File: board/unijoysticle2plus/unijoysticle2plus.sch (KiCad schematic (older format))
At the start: 39 parts, among them J1 DB9_Female, J2 DB9_Female, J3 USB_B_Micro, Q1 MUN5211DW1, SW1 RESET, SW2 JOY SWAP, SW3 BOOT, U1 74HC05, U2 74HC05, U3 74HC05, U4 ESP32-WROOM-32D, U5 AMS1117-3.3, U6 CH340C

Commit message: unijoysticle2plus: rev C
Rev C submitted to JLCPCB.
Added missing JLCPCB parts
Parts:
- C10: LCSC (none) -> C28323
- Q1: LCSC (none) -> C152507
- R5, R6: value 1K -> 1k
- U4: value ESP32-WROOM-32D -> ESP32-WROOM-32E; LCSC C473012 -> C701342
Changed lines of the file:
@@
 P 5250 2750
 F 0 "U4" H 5800 1350 50  0000 C CNN
-F 1 "ESP32-WROOM-32D" H 5850 1250 50  0000 C CNN
+F 1 "ESP32-WROOM-32E" H 5850 1250 50  0000 C CNN
 F 2 "RF_Module:ESP32-WROOM-32" H 5250 1250 50  0001 C CNN
 F 3 "https://www.espressif.com/sites/default/files/documentation/esp32-wroom-32d_esp32-wroom-32u_datasheet_en.pdf" H 4950 2800 50  0001 C CNN
-F 4 "C473012" H 5250 2750 50  0001 C CNN "LCSC"
+F 4 "C701342" H 5250 2750 50  0001 C CNN "LCSC"
 	1    5250 2750
 	1    0    0    -1
@@
 P 10180 2340
 F 0 "R5" V 10040 2340 50  0000 C CNN
-F 1 "1K" V 10110 2340 50  0000 C CNN
+F 1 "1k" V 10110 2340 50  0000 C CNN
 F 2 "Resistor_SMD:R_0805_2012Metric_Pad1.20x1.40mm_HandSolder" H 10180 2340 50  0001 C CNN
 F 3 "~" H 10180 2340 50  0001 C CNN
@@
 P 10180 2440
 F 0 "R6" V 10250 2440 50  0000 C CNN
-F 1 "1K" V 10310 2440 50  0000 C CNN
+F 1 "1k" V 10310 2440 50  0000 C CNN
 F 2 "Resistor_SMD:R_0805_2012Metric_Pad1.20x1.40mm_HandSolder" H 10180 2440 50  0001 C CNN
 F 3 "~" H 10180 2440 50  0001 C CNN
@@
 F 2 "Package_TO_SOT_SMD:SOT-363_SC-70-6" H 7825 4390 50  0001 C CNN
 F 3 "http://www.onsemi.com/pub/Collateral/DTC114ED-D.PDF" H 7820 4830 50  0001 C CNN
+F 4 "C152507" H 7820 4830 50  0001 C CNN "LCSC"
 	1    7820 4830
 	1    0    0    1
@@
 Wire Wire Line
 	8800 1950 8800 1980
-$Comp
-L Device:C_Small C10
-U 1 1 61070B93
-P 8990 2080
-F 0 "C10" H 9082 2126 50  0000 L CNN
-F 1 "1uF" H 9082 2035 50  0000 L CNN
-F 2 "Capacitor_SMD:C_0805_2012Metric_Pad1.18x1.45mm_HandSolder" H 8990 2080 50  0001 C CNN
-F 3 "~" H 8990 2080 50  0001 C CNN
-	1    8990 2080
-	1    0    0    -1
-$EndComp
 Wire Wire Line
 	8990 2180 8990 2210
@@
 	1    0    0    -1
 $EndComp
+$Comp
+L Device:C_Small C10
+U 1 1 61070B93
+P 8990 2080
+F 0 "C10" H 9082 2126 50  0000 L CNN
+F 1 "1uF" H 9082 2035 50  0000 L CNN
+F 2 "Capacitor_SMD:C_0805_2012Metric_Pad1.18x1.45mm_HandSolder" H 8990 2080 50  0001 C CNN
+F 3 "~" H 8990 2080 50  0001 C CNN
+F 4 "C28323" H 8990 2080 50  0001 C CNN "LCSC"
+	1    8990 2080
+	1    0    0    -1
+$EndComp

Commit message: Unijoysticle2+: Rev D
- Swap GPIO 12 & 13: issue #19
- Ground GPIO 4. This is to detect Uni2+
- Back to USB Micro B connector used in Rev. B
  - This is to avoid hand-soldering it.
  - Re-added the "hole" in PCB so that it can be placed using P&P
    machine.
- Reduced Green LED resistor from 1k to 330, this is to make it
  brighter.
- Auto reset circuit wasn't working on Rev C.
  Replaced it with original design, using S8050s.
  Fixed the pins, was broken in Rev A and Rev B.
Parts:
- removed Q1: MUN5211DW1, Package_TO_SOT_SMD:SOT-363_SC-70-6, symbol Transistor_BJT:MUN5211DW1
- added Q1, Q2: S8050, Package_TO_SOT_SMD:SOT-23, symbol Device:Q_NPN_BEC
- added R7, R8: 10k, Resistor_SMD:R_0805_2012Metric_Pad1.20x1.40mm_HandSolder, symbol Device:R_Small
- J3: footprint Unijoysticle:MicroXNJ -> Connector_USB:USB_Micro-B_Molex_47346-0001; LCSC C404969 -> C132560
- R3: value 1k -> 330; LCSC C17513 -> C17630
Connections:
- wire segments 193 -> 198
- no-connect marks 19 -> 18
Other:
- note added: "Differenciates between\nUnijoysticle2 and Unijoysticle2+.\nTo only have one firmware"
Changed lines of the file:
@@
 Sheet 1 1
 Title "Unijoysticle 2+"
-Date "2021-06-25"
-Rev "C"
+Date "2021-07-24"
+Rev "D"
 Comp "Retro Moe"
 Comment1 ""
@@
 Text Label 6650 2050 2    50   ~ 0
 GPIO_J1_LED
-Text Label 6650 2250 2    50   ~ 0
+Text Label 6650 2150 2    50   ~ 0
 GPIO_J2_LED
 Text Label 6650 2450 2    50   ~ 0
@@
 Text Label 6650 3350 2    50   ~ 0
 GPIO_J1_UP
-Text Label 6650 2150 2    50   ~ 0
+Text Label 6650 2250 2    50   ~ 0
 GPIO_J2_FIRE
 Text Label 6650 2350 2    50   ~ 0
@@
 Text Label 6650 1950 2    50   ~ 0
 GPIO04
-Wire Wire Line
-	7130 2850 7130 2750
 Text Label 7860 2350 2    50   ~ 0
 USBD+
@@
 	1    0    0    -1
 $EndComp
-Wire Wire Line
-	7920 4480 7380 4480
-Wire Wire Line
-	7380 4480 7380 4830
-Connection ~ 7380 4830
-Wire Wire Line
-	7280 4280 7280 4630
-Wire Wire Line
-	7280 4280 6980 4280
-Connection ~ 7280 4280
-Wire Wire Line
-	6980 4830 7380 4830
-$Comp
-L Connector:USB_B_Micro J3
-U 1 1 5F99FD12
-P 7130 2350
-F 0 "J3" H 7187 2817 50  0000 C CNN
-F 1 "USB_B_Micro" H 7187 2726 50  0000 C CNN
-F 2 "Unijoysticle:MicroXNJ" H 7280 2300 50  0001 C CNN
-F 3 "~" H 7280 2300 50  0001 C CNN
-F 4 "C404969" H 7130 2350 50  0001 C CNN "LCSC"
-	1    7130 2350
-	1    0    0    -1
-$EndComp
 Text Label 6980 4280 0    50   ~ 0
 DTR_PROG
 Text Label 6980 4830 0    50   ~ 0
 RTS_PROG
-Text Label 8080 5030 0    50   ~ 0
+Text Label 8640 5270 0    50   ~ 0
 ESP_BOOT
-Text Label 8160 4080 0    50   ~ 0
+Text Label 8830 3840 0    50   ~ 0
 ESP_EN
 Wire Wire Line
@@
 GPIO39
 Wire Wire Line
-	9460 5710 9860 5710
-Wire Wire Line
-	9460 5810 9860 5810
-Wire Wire Line
-	9460 5910 9860 5910
-Wire Wire Line
-	9460 6010 9860 6010
-Wire Wire Line
-	9460 6110 9860 6110
-Text Label 9610 6010 0    50   ~ 0
+	10260 5880 10660 5880
+Wire Wire Line
+	10260 5980 10660 5980
+Wire Wire Line
+	10260 6080 10660 6080
+Wire Wire Line
+	10260 6180 10660 6180
+Text Label 10410 6080 0    50   ~ 0
 GPIO36
-Text Label 9610 6110 0    50   ~ 0
+Text Label 10410 6180 0    50   ~ 0
 GPIO39
-Text Label 9610 5710 0    50   ~ 0
+Text Label 8790 5880 0    50   ~ 0
 GPIO04
-Text Label 9610 5810 0    50   ~ 0
+Text Label 10410 5880 0    50   ~ 0
 GPIO34
-Text Label 9610 5910 0    50   ~ 0
+Text Label 10410 5980 0    50   ~ 0
 GPIO35
 Wire Wire Line
@@
 Wire Notes Line
 	6700 550  6700 5500
-Wire Wire Line
-	7280 4630 7870 4630
 $Comp
 L power:+3V3 #PWR013
@@
 Text Notes 550  3650 0    98   ~ 20
 C64 PORTS
-Text Notes 10640 5750 0    98   ~ 20
+Text Notes 10810 5640 0    98   ~ 20
 MISC
 Text Notes 500  4100 0    98   ~ 20
@@
 NoConn ~ 4650 3150
 NoConn ~ 4650 3250
-NoConn ~ 9460 5710
-NoConn ~ 9460 5810
-NoConn ~ 9460 5910
-NoConn ~ 9460 6010
-NoConn ~ 9460 6110
+NoConn ~ 10260 5880
+NoConn ~ 10260 5980
+NoConn ~ 10260 6080
+NoConn ~ 10260 6180
 $Comp
 L Graphic:Logo_Open_Hardware_Small #LOGO1
@@
 P 6550 6000
 F 0 "R3" V 6620 6000 50  0000 C CNN
-F 1 "1k" V 6460 6000 50  0000 C CNN
+F 1 "330" V 6460 6000 50  0000 C CNN
 F 2 "Resistor_SMD:R_0805_2012Metric_Pad1.20x1.40mm_HandSolder" V 6480 6000 50  0001 C CNN
 F 3 "~" H 6550 6000 50  0001 C CNN
-F 4 "C17513" V 6550 6000 50  0001 C CNN "LCSC"
+F 4 "C17630" V 6550 6000 50  0001 C CNN "LCSC"
 	1    6550 6000
 	0    -1   -1   0
@@
 	4100 1800 4100 1840
 Connection ~ 4100 1550
-Text Notes 9120 6310 0    50   ~ 0
+Text Notes 9920 6380 0    50   ~ 0
 Available GPIOs for future use.\nGPIOs 34-39 are Input only
 Wire Wire Line
@@
 	0    -1   -1   0
 $EndComp
-$Comp
-L Transistor_BJT:MUN5211DW1 Q1
-U 2 1 60E74B41
-P 7870 4280
-F 0 "Q1" H 8011 4326 50  0000 L CNN
-F 1 "MUN5211DW1" H 8011 4235 50  0000 L CNN
-F 2 "Package_TO_SOT_SMD:SOT-363_SC-70-6" H 7875 3840 50  0001 C CNN
-F 3 "http://www.onsemi.com/pub/Collateral/DTC114ED-D.PDF" H 7870 4280 50  0001 C CNN
-	2    7870 4280
-	1    0    0    -1
-$EndComp
-$Comp
-L Transistor_BJT:MUN5211DW1 Q1
-U 1 1 60E75D85
-P 7820 4830
-F 0 "Q1" H 7961 4784 50  0000 L CNN
-F 1 "MUN5211DW1" H 7961 4875 50  0000 L CNN
-F 2 "Package_TO_SOT_SMD:SOT-363_SC-70-6" H 7825 4390 50  0001 C CNN
-F 3 "http://www.onsemi.com/pub/Collateral/DTC114ED-D.PDF" H 7820 4830 50  0001 C CNN
-F 4 "C152507" H 7820 4830 50  0001 C CNN "LCSC"
-	1    7820 4830
-	1    0    0    1
-$EndComp
-Wire Wire Line
-	7870 5030 8450 5030
-Wire Wire Line
-	7380 4830 7470 4830
-Wire Wire Line
-	7280 4280 7520 4280
 Wire Wire Line
 	9610 2010 9610 2140
@@
 	1    0    0    -1
 $EndComp
-Wire Wire Line
-	7920 4080 8430 4080
 NoConn ~ 7030 2750
 $Comp
@@
 	1    0    0    -1
 $EndComp
+Wire Wire Line
+	6980 4830 7450 4830
+Wire Wire Line
+	6980 4280 7420 4280
+$Comp
+L Device:R_Small R7
+U 1 1 6103A444
+P 7640 4280
+F 0 "R7" V 7580 4280 50  0000 C CNN
+F 1 "10k" V 7710 4280 50  0000 C CNN
+F 2 "Resistor_SMD:R_0805_2012Metric_Pad1.20x1.40mm_HandSolder" H 7640 4280 50  0001 C CNN
+F 3 "~" H 7640 4280 50  0001 C CNN
+F 4 "C17414" V 7640 4280 50  0001 C CNN "LCSC"
+	1    7640 4280
+	0    1    1    0
+$EndComp
+$Comp
+L Device:R_Small R8
+U 1 1 6103B159
+P 7640 4830
+F 0 "R8" V 7570 4830 50  0000 C CNN
+F 1 "10k" V 7720 4830 50  0000 C CNN
+F 2 "Resistor_SMD:R_0805_2012Metric_Pad1.20x1.40mm_HandSolder" H 7640 4830 50  0001 C CNN
+F 3 "~" H 7640 4830 50  0001 C CNN
+F 4 "C17414" V 7640 4830 50  0001 C CNN "LCSC"
+	1    7640 4830
+	0    1    1    0
+$EndComp
+Wire Wire Line
+	7740 4280 8040 4280
+Wire Wire Line
+	7740 4830 8040 4830
+Wire Wire Line
+	8340 5030 8340 5270
+Wire Wire Line
+	8340 5270 9000 5270
+Wire Wire Line
+	8340 4080 8340 3840
+Wire Wire Line
+	8340 3840 9100 3840
+Connection ~ 7420 4280
+Wire Wire Line
+	7420 4280 7540 4280
+Wire Wire Line
+	7450 4830 7450 4480
+Wire Wire Line
+	7450 4480 8340 4480
+Connection ~ 7450 4830
+Wire Wire Line
+	7450 4830 7540 4830
+Wire Wire Line
+	8340 4630 7420 4630
+Wire Wire Line
+	7420 4280 7420 4630
+$Comp
+L Device:Q_NPN_BEC Q1
+U 1 1 6114C279
+P 8240 4280
+F 0 "Q1" H 8430 4326 50  0000 L CNN
+F 1 "S8050" H 8430 4235 50  0000 L CNN
+F 2 "Package_TO_SOT_SMD:SOT-23" H 8440 4380 50  0001 C CNN
+F 3 "~" H 8240 4280 50  0001 C CNN
+F 4 "C2146" H 8240 4280 50  0001 C CNN "LCSC"
+	1    8240 4280
+	1    0    0    -1
+$EndComp
+$Comp
+L Device:Q_NPN_BEC Q2
+U 1 1 6114CB1B
+P 8240 4830
+F 0 "Q2" H 8430 4876 50  0000 L CNN
+F 1 "S8050" H 8430 4785 50  0000 L CNN
+F 2 "Package_TO_SOT_SMD:SOT-23" H 8440 4930 50  0001 C CNN
+F 3 "~" H 8240 4830 50  0001 C CNN
+F 4 "C2146" H 8240 4830 50  0001 C CNN "LCSC"
+	1    8240 4830
+	1    0    0    -1
+$EndComp
+Wire Wire Line
+	8780 5880 8780 5980
+$Comp
+L power:GND #PWR0113
+U 1 1 61222325
+P 8780 5980
+F 0 "#PWR0113" H 8780 5730 50  0001 C CNN
+F 1 "GND" H 8785 5807 50  0000 C CNN
+F 2 "" H 8780 5980 50  0001 C CNN
+F 3 "" H 8780 5980 50  0001 C CNN
+	1    8780 5980
+	1    0    0    -1
+$EndComp
+Wire Wire Line
+	8780 5880 9060 5880
+Text Notes 8420 5780 0    50   ~ 0
+Differenciates between\nUnijoysticle2 and Unijoysticle2+.\nTo only have one firmware
+Wire Wire Line
+	7130 2750 7130 2850
+$Comp
+L Connector:USB_B_Micro J3
+U 1 1 6137E281
+P 7130 2350
+F 0 "J3" H 7187 2817 50  0000 C CNN
+F 1 "USB_B_Micro" H 7187 2726 50  0000 C CNN
+F 2 "Connector_USB:USB_Micro-B_Molex_47346-0001" H 7280 2300 50  0001 C CNN
+F 3 "~" H 7280 2300 50  0001 C CNN
+F 4 "C132560" H 7130 2350 50  0001 C CNN "LCSC"
+	1    7130 2350
+	1    0    0    -1
+$EndComp

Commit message: unijoysticle2+: place 1000uF cap differently
- Change footprint of 1000uF: bigger
- Place it slightly differently
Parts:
- C7: footprint Capacitor_SMD:CP_Elec_8x10 -> Capacitor_SMD:CP_Elec_10x10; LCSC C134755 -> C249594
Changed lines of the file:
@@
 F 0 "C7" H 6200 1100 50  0000 L CNN
 F 1 "1000uF" H 6150 1000 50  0000 L CNN
-F 2 "Capacitor_SMD:CP_Elec_8x10" H 6400 1050 50  0001 C CNN
+F 2 "Capacitor_SMD:CP_Elec_10x10" H 6400 1050 50  0001 C CNN
 F 3 "~" H 6400 1050 50  0001 C CNN
-F 4 "C134755" H 6400 1050 50  0001 C CNN "LCSC"
+F 4 "C249594" H 6400 1050 50  0001 C CNN "LCSC"
 	1    6400 1050
 	1    0    0    -1

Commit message: Unijosyticle2+: ESP32-WROOM-32E Out-of-Stock, using D
JLCPCB doesn't have WROOM-32E in stock.
Switching back to 32D
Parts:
- U4: LCSC C701342 -> C473012
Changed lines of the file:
@@
 F 2 "RF_Module:ESP32-WROOM-32" H 5250 1250 50  0001 C CNN
 F 3 "https://www.espressif.com/sites/default/files/documentation/esp32-wroom-32d_esp32-wroom-32u_datasheet_en.pdf" H 4950 2800 50  0001 C CNN
-F 4 "C701342" H 5250 2750 50  0001 C CNN "LCSC"
+F 4 "C473012" H 5250 2750 50  0001 C CNN "LCSC"
 	1    5250 2750
 	1    0    0    -1

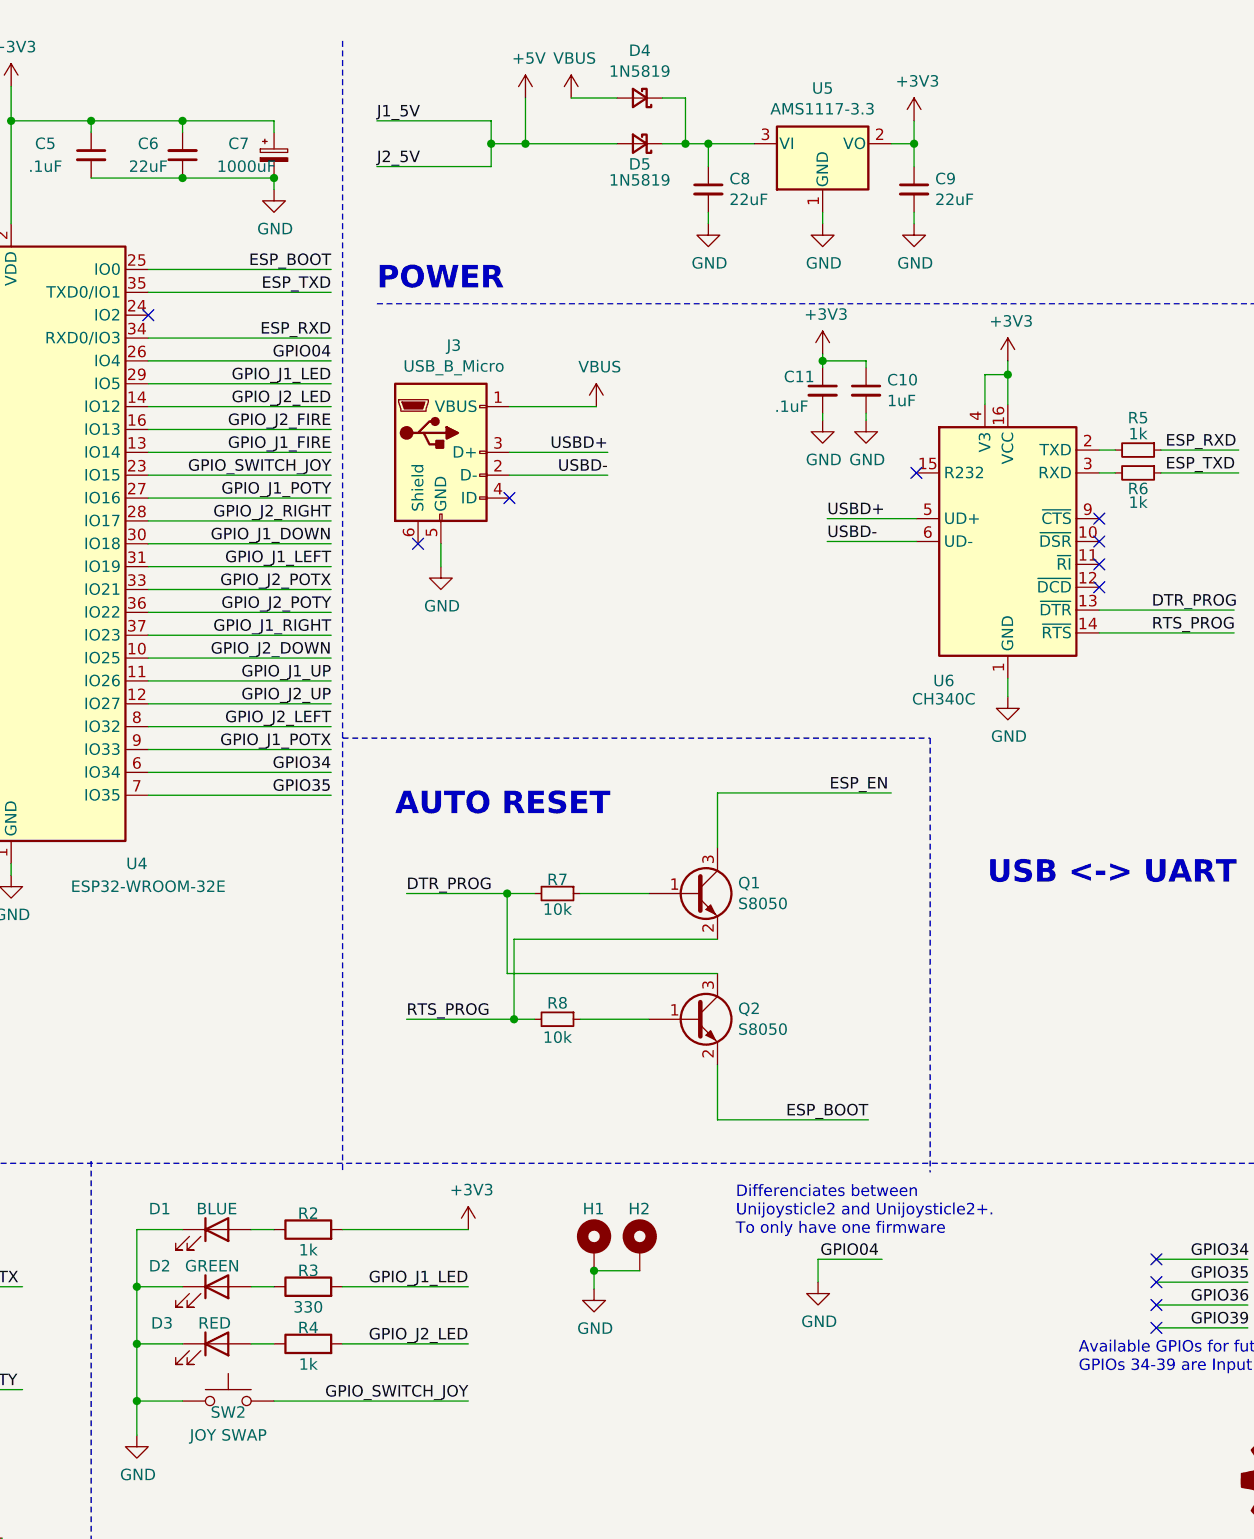
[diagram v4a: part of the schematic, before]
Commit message: Unijoysticle2+: Rev E
- Auto-reset circuit fixed: Transitor lines connected correctly
- Filter cap is between 5v and GND (and not +3.v3 and GND)
- Using 1.5K Ohm resistors for blue and red LEDs instead of 1K
- USB connector is just a tiny bit moved inwards
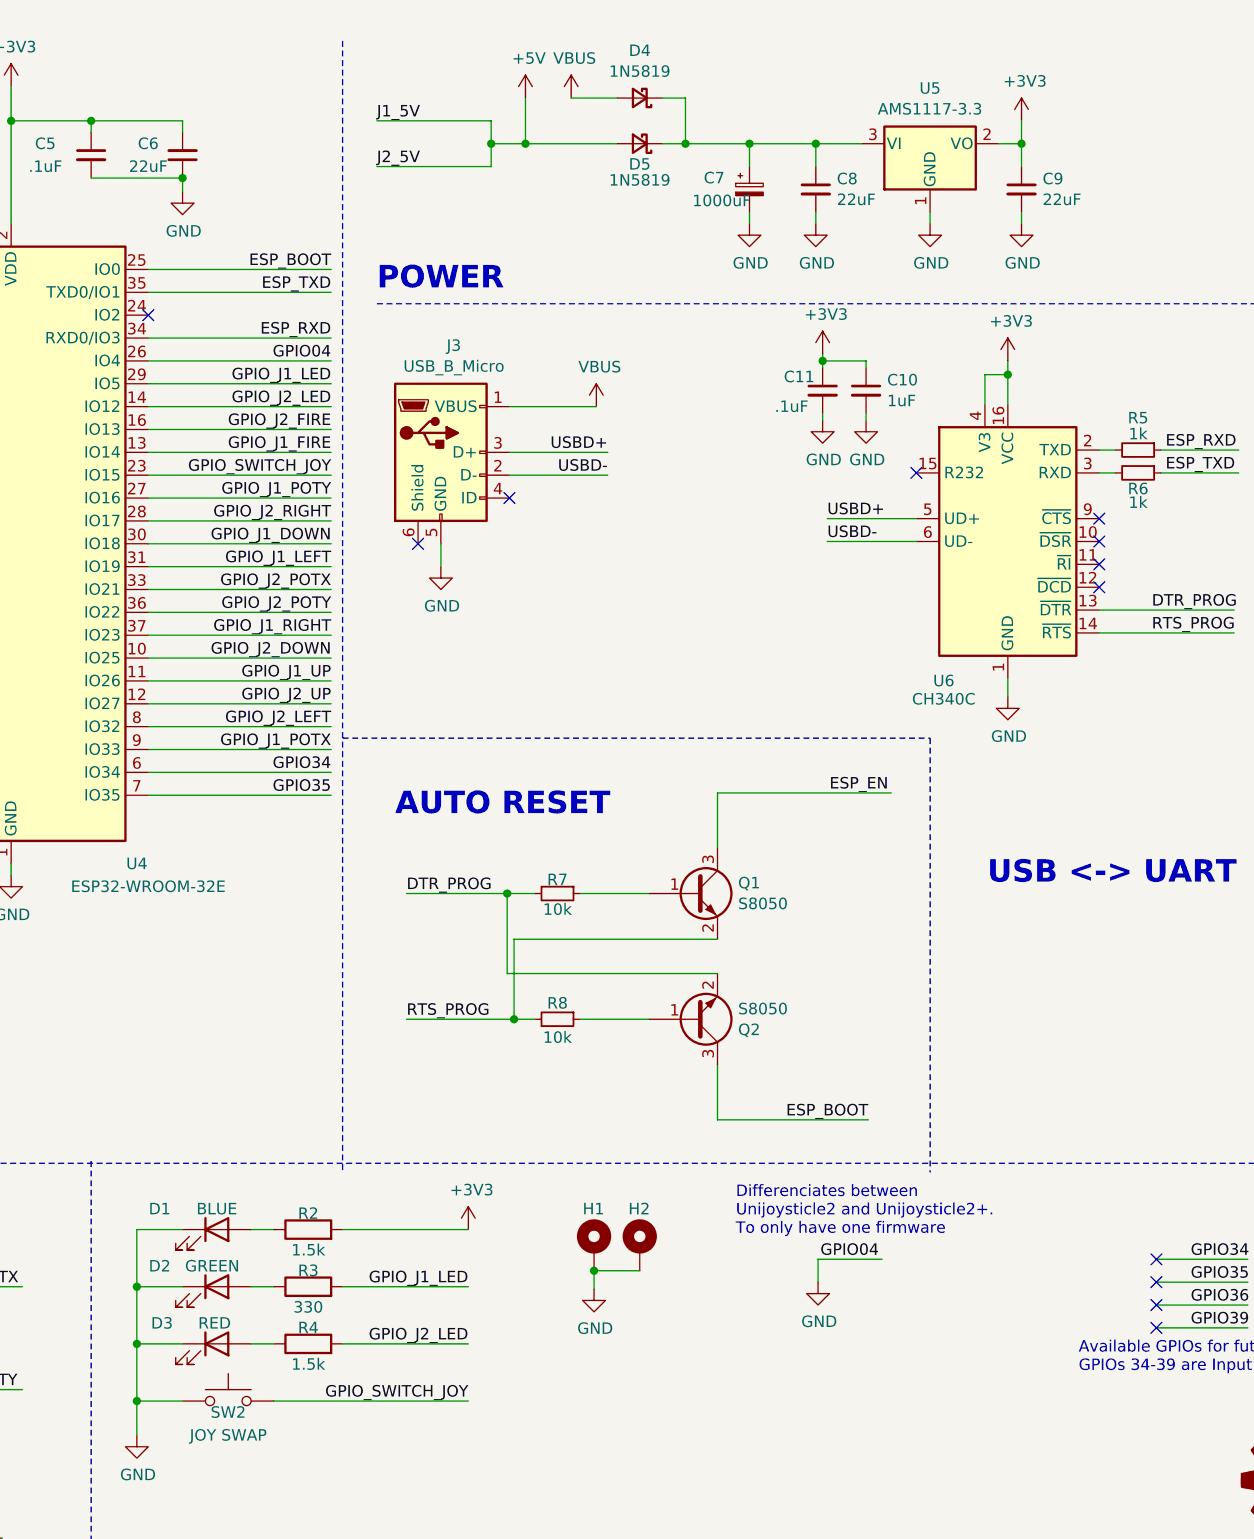
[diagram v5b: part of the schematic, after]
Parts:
- D4, D5: footprint Diode_SMD:D_SMA -> Diode_SMD:D_SOD-123; LCSC C2480 -> C82544
- R2, R4: value 1k -> 1.5k; LCSC C17513 -> C4310
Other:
- moved on the sheet: C7, C8, C9, U5

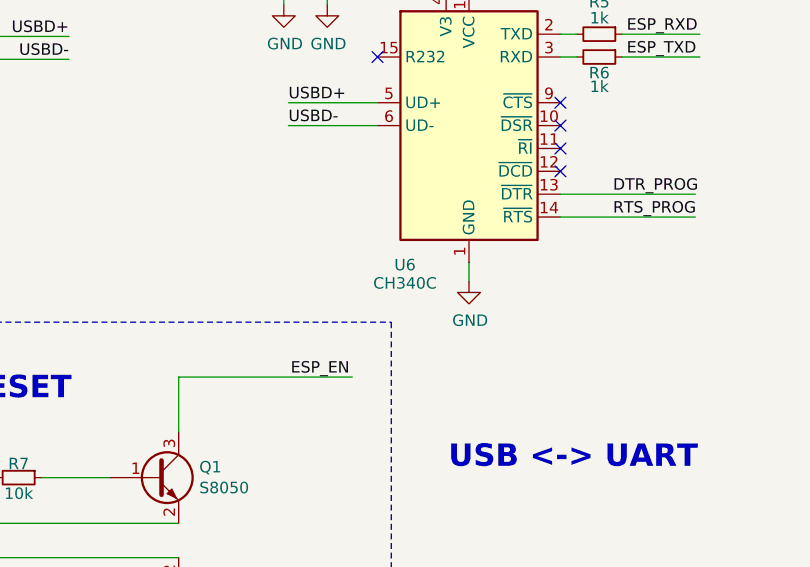
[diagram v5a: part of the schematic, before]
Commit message: Unijoysticle2+: Using CH340B instead of CH340C
CH340C is out of stock in JLCPCB. Using CH340B which is pin-compatible.
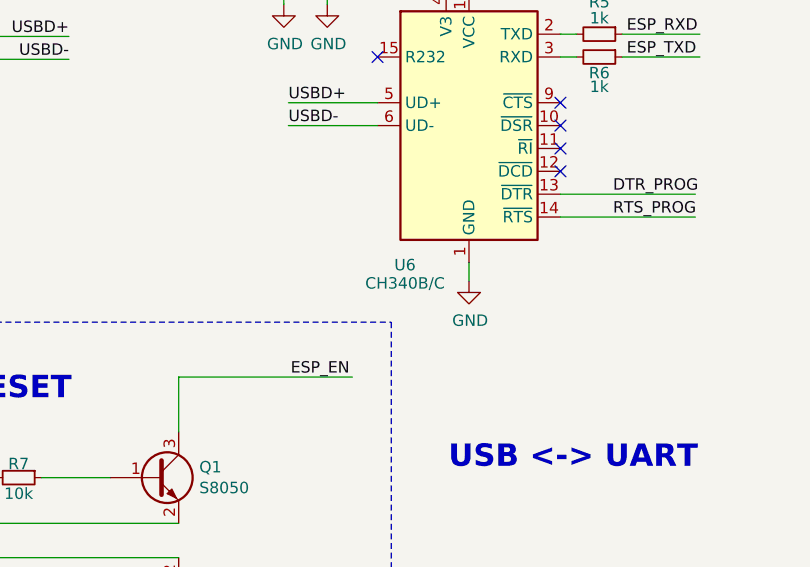
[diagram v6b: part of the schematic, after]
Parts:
- U6: value CH340C -> CH340B/C; LCSC C84681 -> C81010
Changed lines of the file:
@@
 P 9610 2740
 F 0 "U6" H 9330 2130 50  0000 C CNN
-F 1 "CH340C" H 9330 2050 50  0000 C CNN
+F 1 "CH340B/C" H 9330 2050 50  0000 C CNN
 F 2 "Package_SO:SOIC-16_3.9x9.9mm_P1.27mm" H 9660 2190 50  0001 L CNN
 F 3 "https://datasheet.lcsc.com/szlcsc/Jiangsu-Qin-Heng-CH340C_C84681.pdf" H 9260 3540 50  0001 C CNN
-F 4 "C84681" H 9610 2740 50  0001 C CNN "LCSC"
+F 4 "C81010" H 9610 2740 50  0001 C CNN "LCSC"
 	1    9610 2740
 	1    0    0    -1
